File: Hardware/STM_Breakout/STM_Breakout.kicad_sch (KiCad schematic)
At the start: 18 parts, among them J1 Conn_01x12_Pin, SW1 SW_Push, U1 STM32F042F6Px, U2 ATA6561

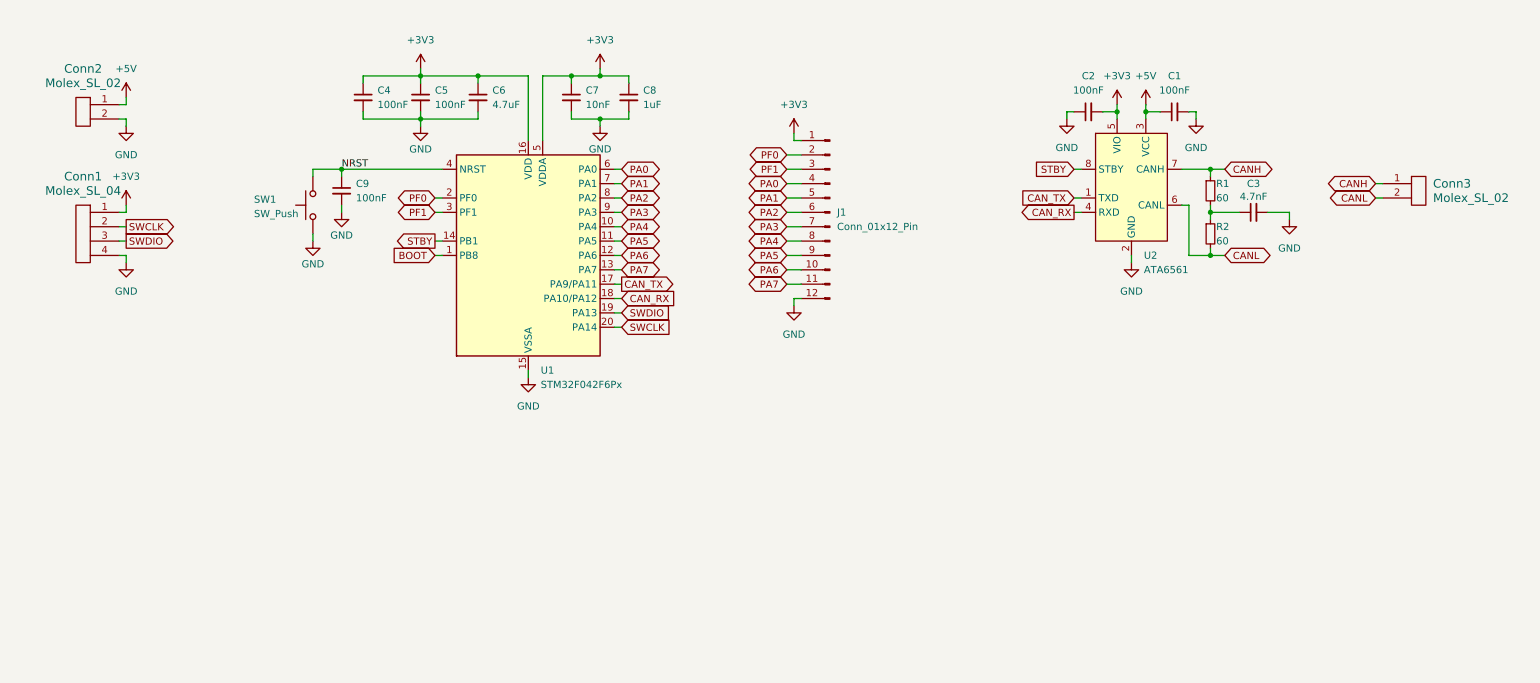
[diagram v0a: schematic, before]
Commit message: Finish STM Breakout Schematic
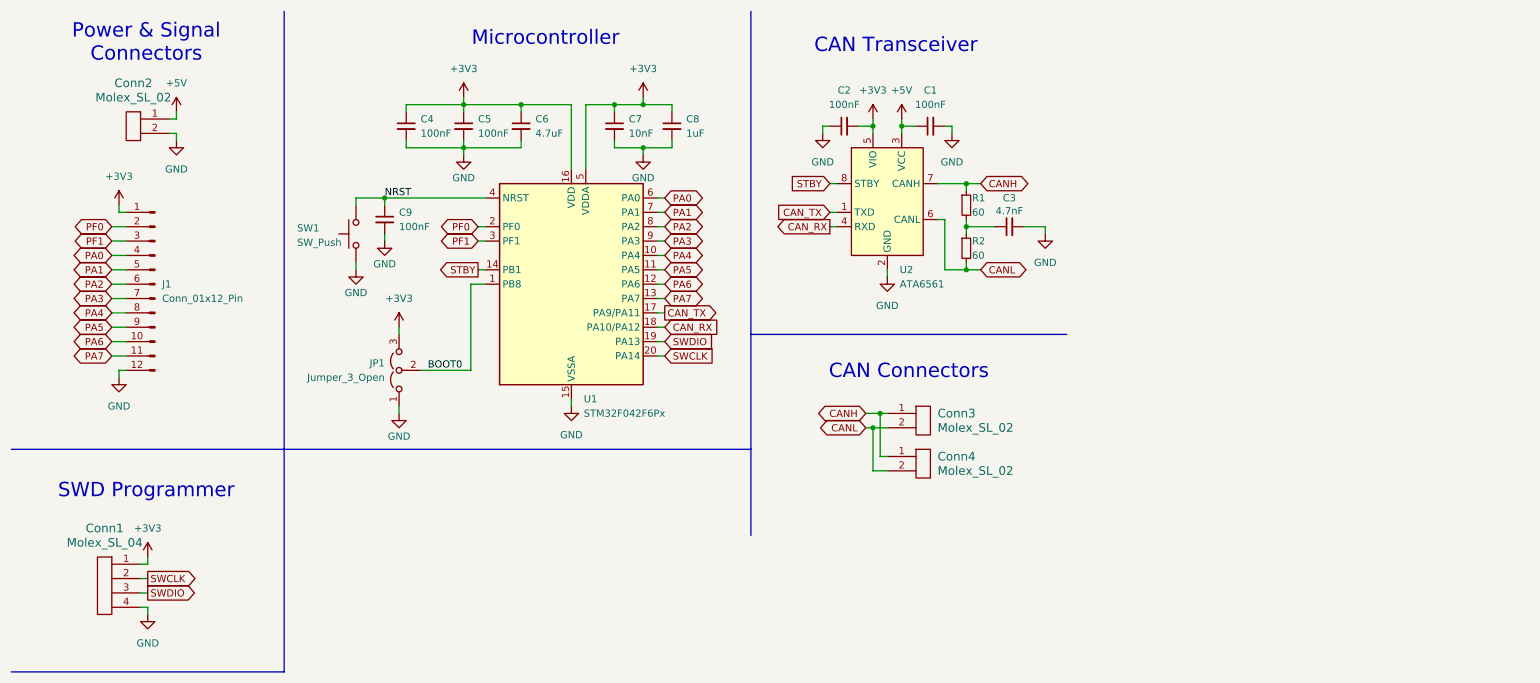
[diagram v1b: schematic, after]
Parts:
- added Conn4: Molex_SL_02, symbol MRDT_Connectors:Molex_SL_02
- added JP1: Jumper_3_Open, symbol Jumper:Jumper_3_Open
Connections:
- net +3V3: now also JP1.3 (B)
- net CANH: now also Conn4.1
- net CANL: now also Conn4.2
- net GND: now also JP1.1 (A)
- net BOOT renamed BOOT0
- net BOOT0: now also JP1.2 (C)
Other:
- note added: "CAN Connectors"
- note added: "CAN Transceiver"
- note added: "Microcontroller"
- note added: "Power & Signal Connectors"
- note added: "SWD Programmer"
- moved on the sheet: C1, C2, C3, C4, C5, C6, C7, C8, C9, Conn1, Conn2, Conn3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

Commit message: Footprint assignments for STM Breakout
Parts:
- C1, C2, C3, C4, C5, C6, C7, C8, C9: footprint (none) -> Capacitor_SMD:C_0603_1608Metric_Pad1.08x0.95mm_HandSolder
- Conn1: footprint (none) -> MRDT_Connectors:MOLEX_SL_04_Vertical
- Conn2, Conn3, Conn4: footprint (none) -> MRDT_Connectors:MOLEX_SL_02_Vertical
- J1: footprint (none) -> Connector_PinHeader_1.00mm:PinHeader_1x12_P1.00mm_Vertical
- JP1: footprint (none) -> Connector_PinHeader_1.00mm:PinHeader_1x03_P1.00mm_Vertical
- R1, R2: footprint (none) -> Resistor_SMD:R_0603_1608Metric_Pad0.98x0.95mm_HandSolder
- SW1: footprint (none) -> Button_Switch_SMD:SW_SPST_TL3305A
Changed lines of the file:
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@@
 			)
 		)
-		(property "Footprint" ""
+		(property "Footprint" "Capacitor_SMD:C_0603_1608Metric_Pad1.08x0.95mm_HandSolder"
 			(at 128.27 31.75 0)
 			(effects
@@
 			)
 		)
-		(property "Footprint" ""
+		(property "Footprint" "MRDT_Connectors:MOLEX_SL_02_Vertical"
 			(at 171.45 88.9 0)
 			(effects
@@
 			)
 		)
-		(property "Footprint" ""
+		(property "Footprint" "Capacitor_SMD:C_0603_1608Metric_Pad1.08x0.95mm_HandSolder"
 			(at 81.28 31.75 0)
 			(effects
@@
 			)
 		)
-		(property "Footprint" ""
+		(property "Footprint" "Capacitor_SMD:C_0603_1608Metric_Pad1.08x0.95mm_HandSolder"
 			(at 187.96 49.53 0)
 			(effects
@@
 			)
 		)
-		(property "Footprint" ""
+		(property "Footprint" "Resistor_SMD:R_0603_1608Metric_Pad0.98x0.95mm_HandSolder"
 			(at 180.34 45.72 0)
 			(effects
@@
 			)
 		)
-		(property "Footprint" ""
+		(property "Footprint" "Capacitor_SMD:C_0603_1608Metric_Pad1.08x0.95mm_HandSolder"
 			(at 91.44 31.75 0)
 			(effects
@@
 			)
 		)
-		(property "Footprint" ""
+		(property "Footprint" "MRDT_Connectors:MOLEX_SL_04_Vertical"
 			(at 29.21 118.11 0)
 			(effects
@@
 			)
 		)
-		(property "Footprint" ""
+		(property "Footprint" "Capacitor_SMD:C_0603_1608Metric_Pad1.08x0.95mm_HandSolder"
 			(at 158.75 31.75 0)
 			(effects
@@
 			)
 		)
-		(property "Footprint" ""
+		(property "Footprint" "Button_Switch_SMD:SW_SPST_TL3305A"
 			(at 67.31 50.8 0)
 			(effects
@@
 			)
 		)
-		(property "Footprint" ""
+		(property "Footprint" "Capacitor_SMD:C_0603_1608Metric_Pad1.08x0.95mm_HandSolder"
 			(at 173.99 31.75 0)
 			(effects
@@
 			)
 		)
-		(property "Footprint" ""
+		(property "Footprint" "Capacitor_SMD:C_0603_1608Metric_Pad1.08x0.95mm_HandSolder"
 			(at 77.47 48.26 0)
 			(effects
@@
 			)
 		)
-		(property "Footprint" ""
+		(property "Footprint" "Capacitor_SMD:C_0603_1608Metric_Pad1.08x0.95mm_HandSolder"
 			(at 118.11 31.75 0)
 			(effects
@@
 			)
 		)
-		(property "Footprint" ""
+		(property "Footprint" "Resistor_SMD:R_0603_1608Metric_Pad0.98x0.95mm_HandSolder"
 			(at 180.34 53.34 0)
 			(effects
@@
 			)
 		)
-		(property "Footprint" ""
+		(property "Footprint" "Connector_PinHeader_1.00mm:PinHeader_1x03_P1.00mm_Vertical"
 			(at 80.01 74.93 0)
 			(effects
@@
 			)
 		)
-		(property "Footprint" ""
+		(property "Footprint" "Connector_PinHeader_1.00mm:PinHeader_1x12_P1.00mm_Vertical"
 			(at 36.83 59.69 0)
 			(effects
@@
 			)
 		)
-		(property "Footprint" ""
+		(property "Footprint" "MRDT_Connectors:MOLEX_SL_02_Vertical"
 			(at 171.45 96.52 0)
 			(effects
@@
 			)
 		)
-		(property "Footprint" ""
+		(property "Footprint" "Capacitor_SMD:C_0603_1608Metric_Pad1.08x0.95mm_HandSolder"
 			(at 101.6 31.75 0)
 			(effects
@@
 			)
 		)
-		(property "Footprint" ""
+		(property "Footprint" "MRDT_Connectors:MOLEX_SL_02_Vertical"
 			(at 34.29 36.83 0)
 			(effects

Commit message: Increase header pitch in STM32 breakout
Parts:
- J1: footprint Connector_PinHeader_1.00mm:PinHeader_1x12_P1.00mm_Vertical -> Connector_PinHeader_2.54mm:PinHeader_2x06_P2.54mm_Vertical
- JP1: footprint Connector_PinHeader_1.00mm:PinHeader_1x03_P1.00mm_Vertical -> Connector_PinHeader_2.54mm:PinHeader_1x03_P2.54mm_Vertical
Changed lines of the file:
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@@
 			)
 		)
-		(property "Footprint" "Connector_PinHeader_1.00mm:PinHeader_1x03_P1.00mm_Vertical"
+		(property "Footprint" "Connector_PinHeader_2.54mm:PinHeader_1x03_P2.54mm_Vertical"
 			(at 80.01 74.93 0)
 			(effects
@@
 			)
 		)
-		(property "Footprint" "Connector_PinHeader_1.00mm:PinHeader_1x12_P1.00mm_Vertical"
+		(property "Footprint" "Connector_PinHeader_2.54mm:PinHeader_2x06_P2.54mm_Vertical"
 			(at 36.83 59.69 0)
 			(effects

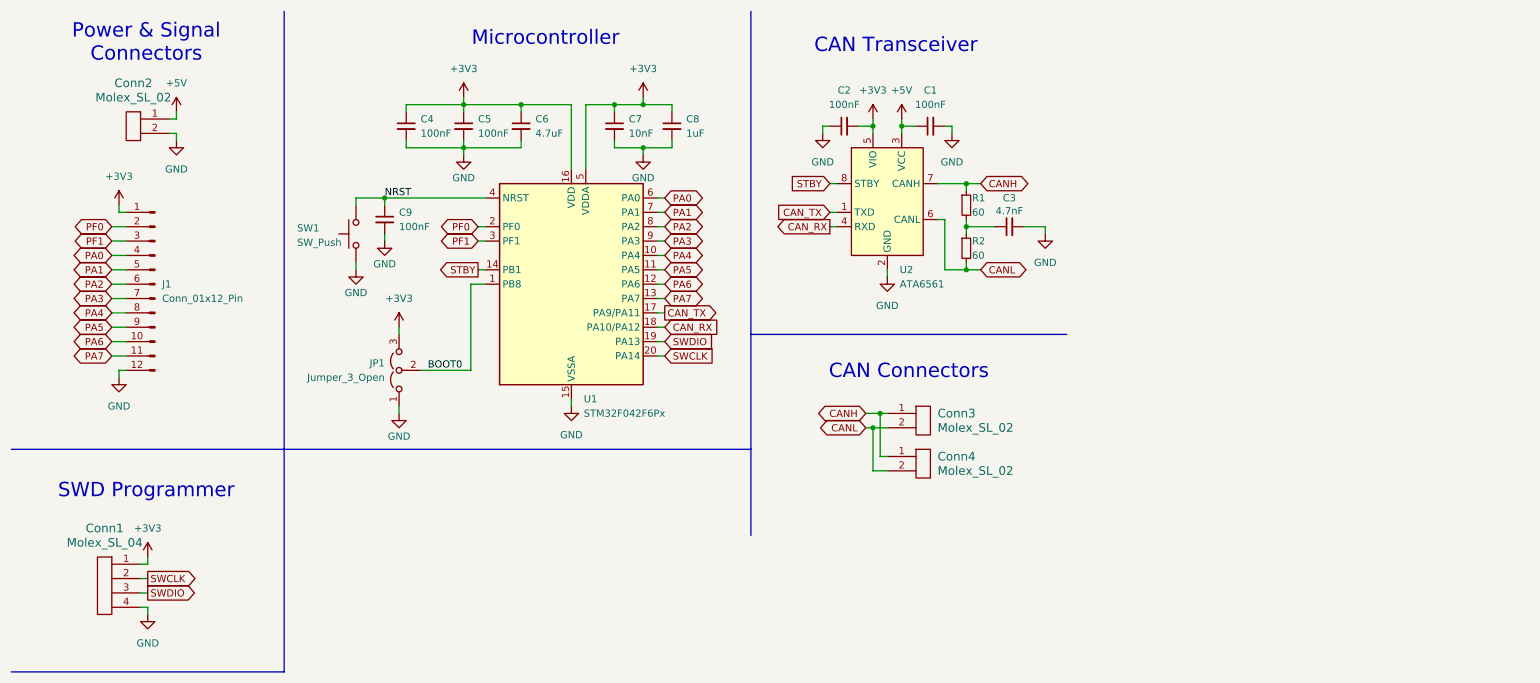
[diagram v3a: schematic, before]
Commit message: Replace reset button with jumper
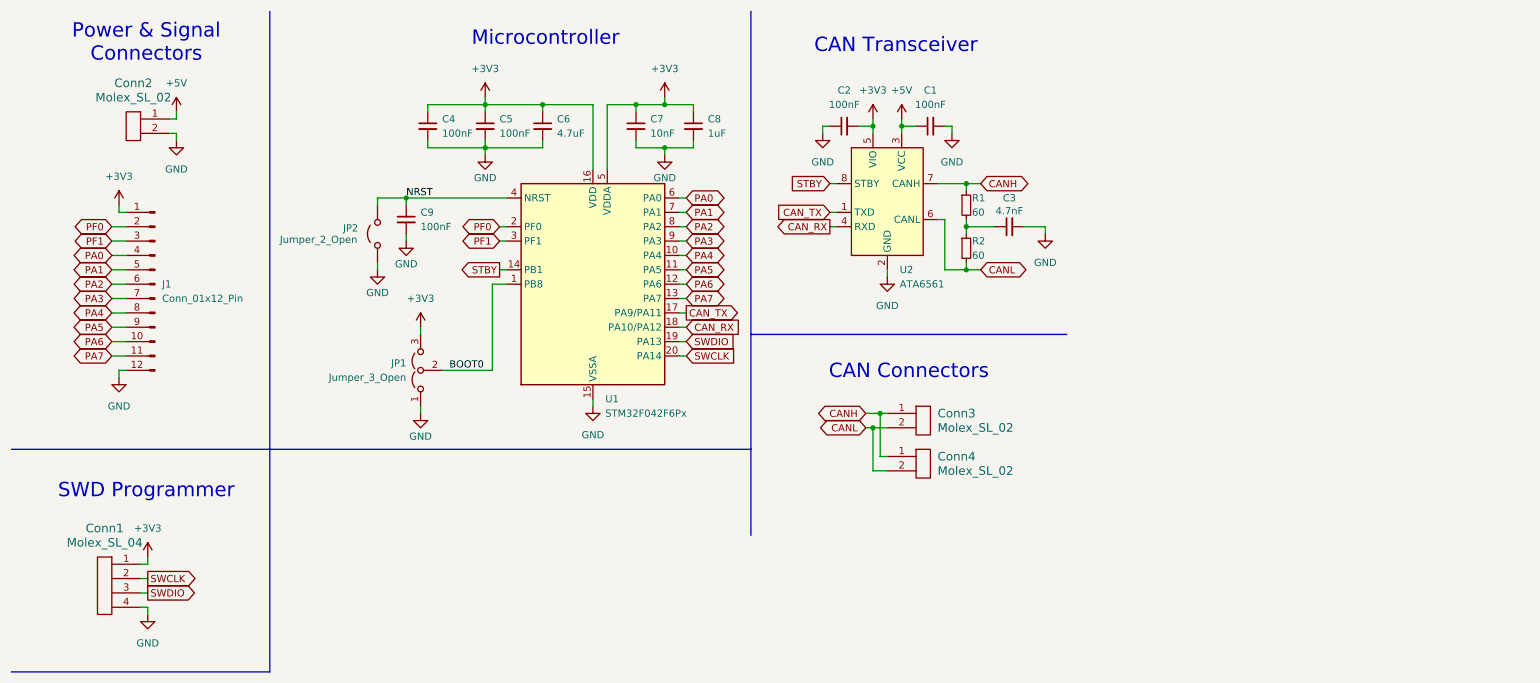
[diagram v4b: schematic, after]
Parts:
- removed SW1: SW_Push, Button_Switch_SMD:SW_SPST_TL3305A, symbol Switch:SW_Push
- added JP2: Jumper_2_Open, Connector_PinHeader_2.54mm:PinHeader_1x02_P2.54mm_Vertical, symbol Jumper:Jumper_2_Open
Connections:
- net GND: now also JP2.2 (B)
- net NRST: now also JP2.1 (A)
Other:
- moved on the sheet: C4, C5, C6, C7, C8, C9, JP1, U1
